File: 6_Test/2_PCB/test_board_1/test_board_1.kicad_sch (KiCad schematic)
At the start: 4 parts, among them U1 TPS74501PDRVR, U2 SN74ALVCH162827DLR, U3 ADA4807-2ARMZ

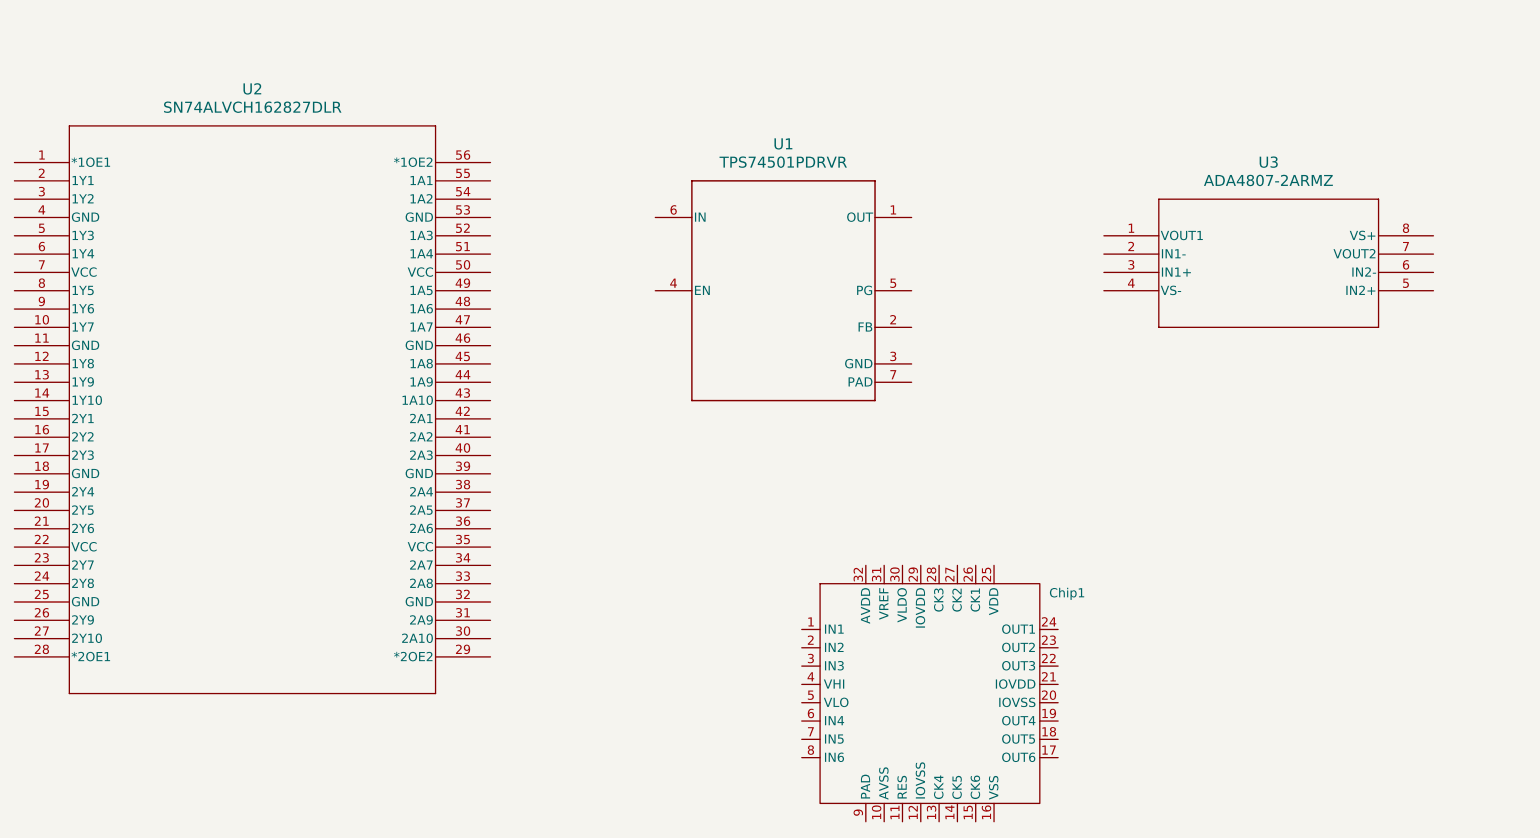
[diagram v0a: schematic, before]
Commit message: added potentiometer model. Split up design into sheets. Progress on analog power supply
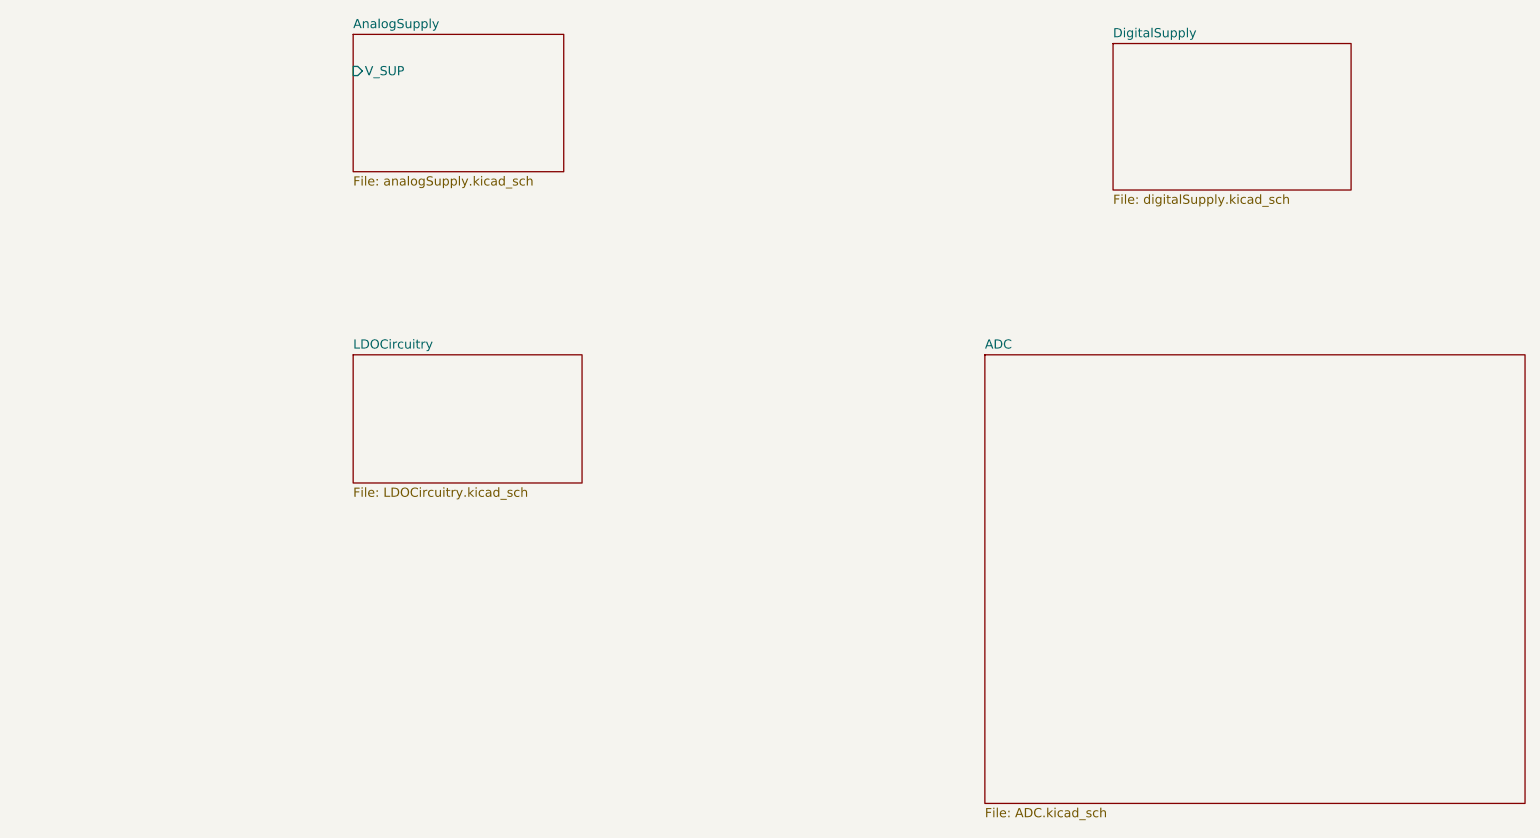
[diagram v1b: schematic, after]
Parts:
- removed Chip1: ~, symbol Chip:Chip
- removed U1: TPS74501PDRVR, TPS74501PDRVR:DRV0006A, symbol TPS74501PDRVR:TPS74501PDRVR
- removed U2: SN74ALVCH162827DLR, SN74ALVCH162827DLR:DL56, symbol 74ALVCH162827DLR:SN74ALVCH162827DLR
- removed U3: ADA4807-2ARMZ, ADA4807-2ARMZ:RM-8_ADI, symbol ADA4807-2ARMZ:ADA4807-2ARMZ
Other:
- added sheet ADC (ADC.kicad_sch)
- added sheet AnalogSupply (analogSupply.kicad_sch)
- added sheet DigitalSupply (digitalSupply.kicad_sch)
- added sheet LDOCircuitry (LDOCircuitry.kicad_sch)

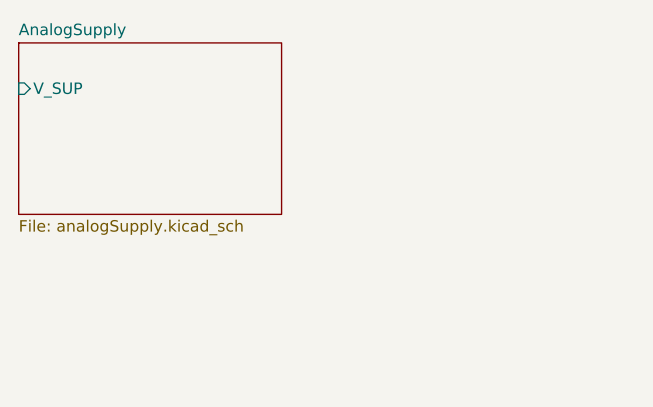
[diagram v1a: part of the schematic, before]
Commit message: progress on analog supply
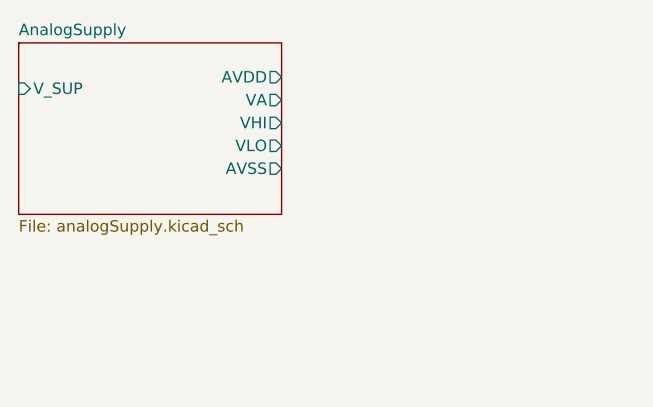
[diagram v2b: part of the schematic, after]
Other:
- sheet AnalogSupply ports: added AVDD, AVSS, VA, VHI, VLO; removed none
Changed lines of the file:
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@@
+			)
+		)
+		(pin "AVDD" output
+			(at 132.08 41.91 0)
+			(effects
+				(font
+					(size 1.27 1.27)
+				)
+				(justify right)
+			)
+		)
+		(pin "VA" output
+			(at 132.08 44.45 0)
+			(effects
+				(font
+					(size 1.27 1.27)
+				)
+				(justify right)
+			)
+		)
+		(pin "AVSS" output
+			(at 132.08 52.07 0)
+			(effects
+				(font
+					(size 1.27 1.27)
+				)
+				(justify right)
+			)
+		)
+		(pin "VHI" output
+			(at 132.08 46.99 0)
+			(effects
+				(font
+					(size 1.27 1.27)
+				)
+				(justify right)
+			)
+		)
+		(pin "VLO" output
+			(at 132.08 49.53 0)
+			(effects
+				(font
+					(size 1.27 1.27)
+				)
+				(justify right)
 			)
 		)
